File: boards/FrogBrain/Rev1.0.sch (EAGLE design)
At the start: 14 parts, among them U1 PIC16F1778, U2 AT25SF321, U3 ADP7104

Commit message: Final rev 1.0 brain and initial tadpole breadboard.
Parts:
- renumbered U$4 to SW
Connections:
- net GND: now also JP4.1, JP4.2, JP4.3, JP5.4, JP5.8
- net SCK: now also JP5.7; no longer JP4.3
- net SI: now also JP5.5; no longer JP4.5
- net SO: now also JP5.6; no longer JP4.4
- net UARTRX: now also JP4.4; no longer JP4.1
- net UARTTX: now also JP4.5; no longer JP4.2
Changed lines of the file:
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@@
 <part name="SUPPLY7" library="supply2" deviceset="GND" device=""/>
 <part name="R2" library="adafruit" deviceset="R-US_" device="R0805" value="100K"/>
-<part name="U$4" library="lib-works" deviceset="PTS645" device=""/>
+<part name="SW" library="lib-works" deviceset="PTS645" device=""/>
 <part name="SUPPLY8" library="supply2" deviceset="GND" device=""/>
 <part name="VDD2" library="supply1" deviceset="VDD" device=""/>
@@
 <instance part="SUPPLY7" gate="GND" x="2.54" y="53.34"/>
 <instance part="R2" gate="G$1" x="-50.8" y="76.2" rot="R90"/>
-<instance part="U$4" gate="G$1" x="-53.34" y="63.5"/>
+<instance part="SW" gate="G$1" x="-53.34" y="63.5"/>
 <instance part="SUPPLY8" gate="GND" x="-50.8" y="50.8"/>
 <instance part="VDD2" gate="G$1" x="-86.36" y="25.4"/>
@@
 </segment>
 <segment>
-<pinref part="U$4" gate="G$1" pin="P$2"/>
+<pinref part="SW" gate="G$1" pin="P$2"/>
 <pinref part="SUPPLY8" gate="GND" pin="GND"/>
-<pinref part="U$4" gate="G$1" pin="P$1"/>
+<pinref part="SW" gate="G$1" pin="P$1"/>
 <wire x1="-50.8" y1="55.88" x2="-53.34" y2="55.88" width="0.1524" layer="91"/>
 <wire x1="-50.8" y1="55.88" x2="-50.8" y2="53.34" width="0.1524" layer="91"/>
@@
 </segment>
 <segment>
-<wire x1="132.08" y1="5.08" x2="114.3" y2="5.08" width="0.1524" layer="91"/>
+<wire x1="132.08" y1="5.08" x2="124.46" y2="5.08" width="0.1524" layer="91"/>
+<wire x1="124.46" y1="5.08" x2="114.3" y2="5.08" width="0.1524" layer="91"/>
 <wire x1="114.3" y1="5.08" x2="114.3" y2="2.54" width="0.1524" layer="91"/>
 <pinref part="SUPPLY9" gate="GND" pin="GND"/>
 <pinref part="JP5" gate="G$1" pin="3"/>
+<pinref part="JP5" gate="G$1" pin="4"/>
+<wire x1="132.08" y1="2.54" x2="124.46" y2="2.54" width="0.1524" layer="91"/>
+<wire x1="124.46" y1="2.54" x2="124.46" y2="5.08" width="0.1524" layer="91"/>
+</segment>
+<segment>
+<wire x1="132.08" y1="43.18" x2="124.46" y2="43.18" width="0.1524" layer="91"/>
+<label x="124.46" y="43.18" size="1.27" layer="95" rot="R180" xref="yes"/>
+<pinref part="JP4" gate="G$1" pin="1"/>
+</segment>
+<segment>
+<wire x1="132.08" y1="40.64" x2="124.46" y2="40.64" width="0.1524" layer="91"/>
+<label x="124.46" y="40.64" size="1.27" layer="95" rot="R180" xref="yes"/>
+<pinref part="JP4" gate="G$1" pin="2"/>
+</segment>
+<segment>
+<wire x1="132.08" y1="38.1" x2="124.46" y2="38.1" width="0.1524" layer="91"/>
+<label x="124.46" y="38.1" size="1.27" layer="95" rot="R180" xref="yes"/>
+<pinref part="JP4" gate="G$1" pin="3"/>
+</segment>
+<segment>
+<pinref part="JP5" gate="G$1" pin="8"/>
+<wire x1="132.08" y1="-7.62" x2="124.46" y2="-7.62" width="0.1524" layer="91"/>
+<label x="124.46" y="-7.62" size="1.27" layer="95" rot="R180" xref="yes"/>
 </segment>
 </net>
@@
 <segment>
 <pinref part="R2" gate="G$1" pin="1"/>
-<pinref part="U$4" gate="G$1" pin="P$4"/>
+<pinref part="SW" gate="G$1" pin="P$4"/>
 <wire x1="-50.8" y1="71.12" x2="-45.72" y2="71.12" width="0.1524" layer="91"/>
 <wire x1="-45.72" y1="71.12" x2="-45.72" y2="73.66" width="0.1524" layer="91"/>
@@
 <wire x1="-45.72" y1="73.66" x2="-40.64" y2="73.66" width="0.1524" layer="91"/>
 <junction x="-50.8" y="71.12"/>
-<pinref part="U$4" gate="G$1" pin="P$3"/>
+<pinref part="SW" gate="G$1" pin="P$3"/>
 <wire x1="-50.8" y1="71.12" x2="-53.34" y2="71.12" width="0.1524" layer="91"/>
 </segment>
@@
 </segment>
 <segment>
-<wire x1="132.08" y1="43.18" x2="124.46" y2="43.18" width="0.1524" layer="91"/>
-<label x="124.46" y="43.18" size="1.27" layer="95" rot="R180" xref="yes"/>
-<pinref part="JP4" gate="G$1" pin="1"/>
+<wire x1="132.08" y1="35.56" x2="124.46" y2="35.56" width="0.1524" layer="91"/>
+<label x="124.46" y="35.56" size="1.27" layer="95" rot="R180" xref="yes"/>
+<pinref part="JP4" gate="G$1" pin="4"/>
 </segment>
 </net>
@@
 </segment>
 <segment>
-<wire x1="132.08" y1="40.64" x2="124.46" y2="40.64" width="0.1524" layer="91"/>
-<label x="124.46" y="40.64" size="1.27" layer="95" rot="R180" xref="yes"/>
-<pinref part="JP4" gate="G$1" pin="2"/>
+<wire x1="132.08" y1="33.02" x2="124.46" y2="33.02" width="0.1524" layer="91"/>
+<label x="124.46" y="33.02" size="1.27" layer="95" rot="R180" xref="yes"/>
+<pinref part="JP4" gate="G$1" pin="5"/>
 </segment>
 </net>
@@
 </segment>
 <segment>
-<wire x1="132.08" y1="38.1" x2="124.46" y2="38.1" width="0.1524" layer="91"/>
-<label x="124.46" y="38.1" size="1.27" layer="95" rot="R180" xref="yes"/>
-<pinref part="JP4" gate="G$1" pin="3"/>
+<pinref part="JP5" gate="G$1" pin="7"/>
+<wire x1="132.08" y1="-5.08" x2="124.46" y2="-5.08" width="0.1524" layer="91"/>
+<label x="124.46" y="-5.08" size="1.27" layer="95" rot="R180" xref="yes"/>
 </segment>
 </net>
@@
 </segment>
 <segment>
-<wire x1="132.08" y1="35.56" x2="124.46" y2="35.56" width="0.1524" layer="91"/>
-<label x="124.46" y="35.56" size="1.27" layer="95" rot="R180" xref="yes"/>
-<pinref part="JP4" gate="G$1" pin="4"/>
+<pinref part="JP5" gate="G$1" pin="6"/>
+<wire x1="132.08" y1="-2.54" x2="124.46" y2="-2.54" width="0.1524" layer="91"/>
+<label x="124.46" y="-2.54" size="1.27" layer="95" rot="R180" xref="yes"/>
 </segment>
 </net>
@@
 </segment>
 <segment>
-<wire x1="132.08" y1="33.02" x2="124.46" y2="33.02" width="0.1524" layer="91"/>
-<label x="124.46" y="33.02" size="1.27" layer="95" rot="R180" xref="yes"/>
-<pinref part="JP4" gate="G$1" pin="5"/>
-</segment>
-</net>
+<pinref part="JP5" gate="G$1" pin="5"/>
+<wire x1="132.08" y1="0" x2="124.46" y2="0" width="0.1524" layer="91"/>
+<label x="124.46" y="0" size="1.27" layer="95" rot="R180" xref="yes"/>
+</segment>
+</net>

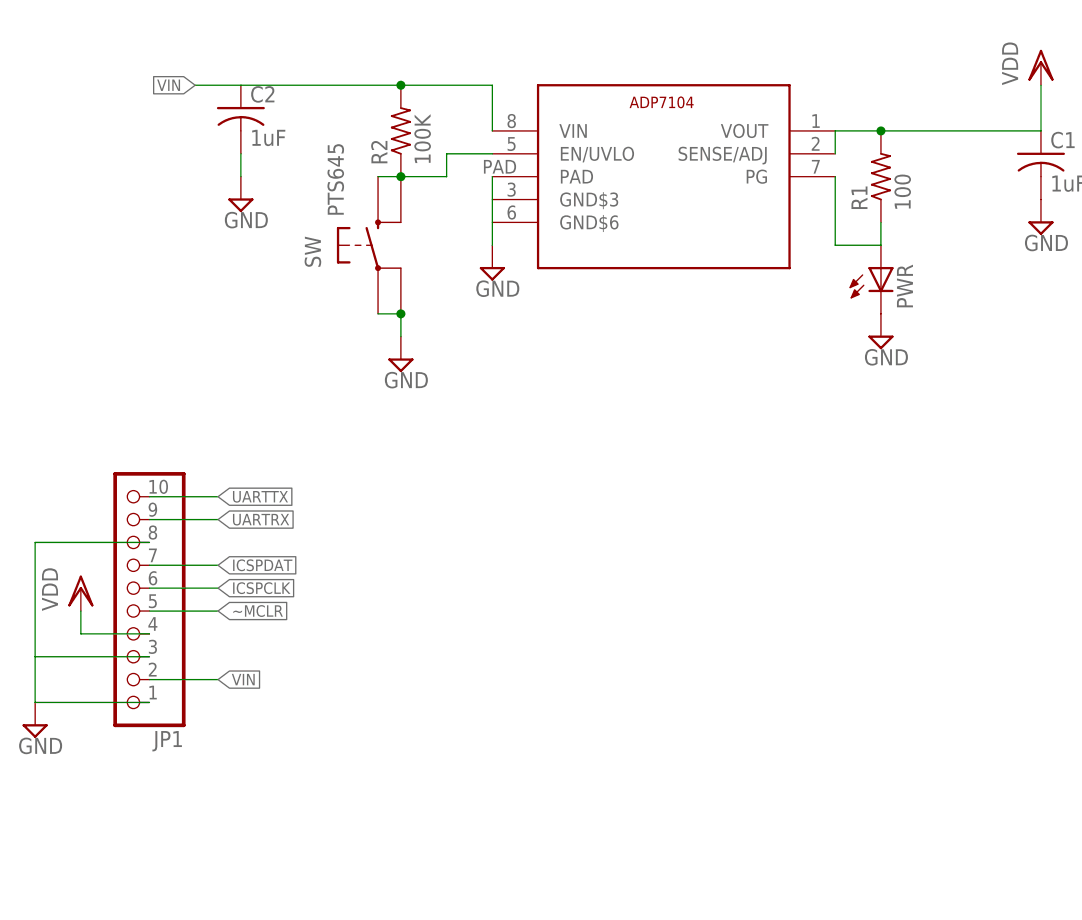
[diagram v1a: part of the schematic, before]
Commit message: Kermit PIC protocol and small frogbrain board mods.
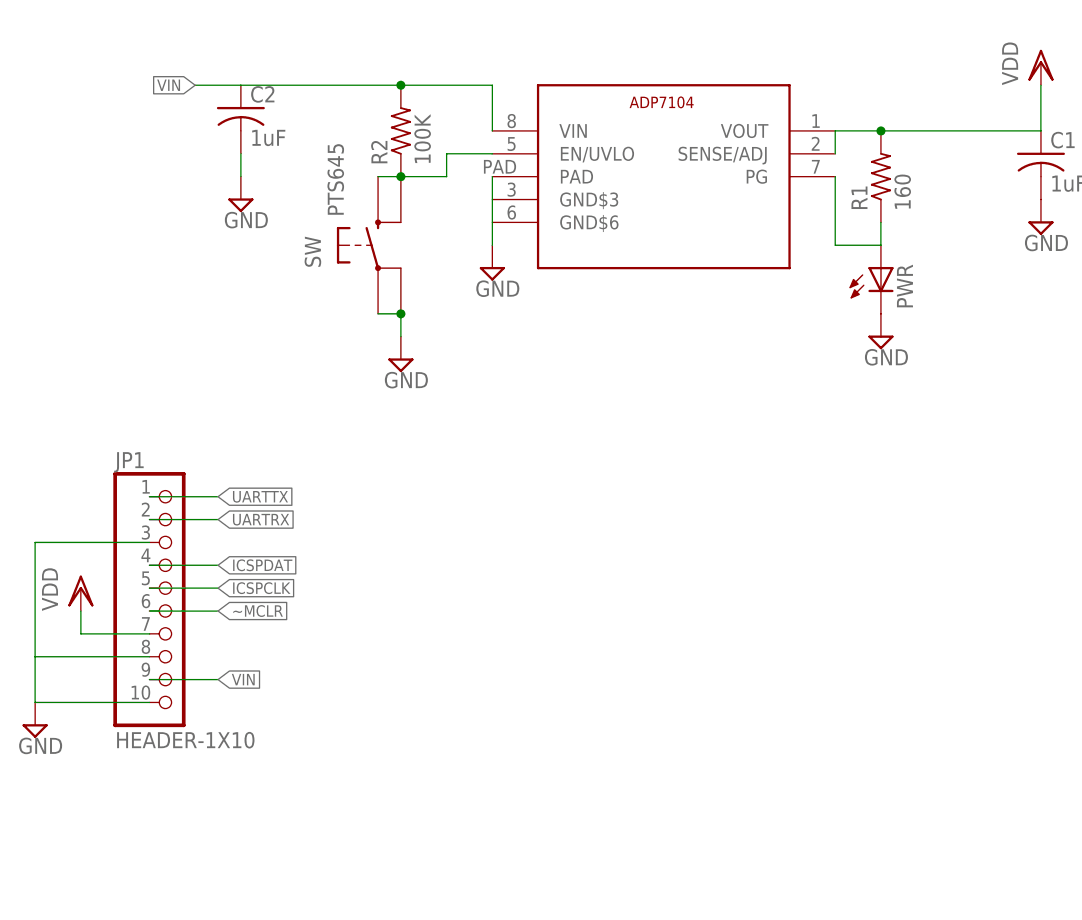
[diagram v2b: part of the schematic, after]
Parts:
- JP1: value (none) -> HEADER-1X10; device pinhead:PINHD-1X10 -> lib-works:HEADER-1X10
- R1: value 100 -> 160
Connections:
- net GND: now also JP1.10; no longer JP1.1
- net ICSPCLK: now also JP1.5; no longer JP1.6
- net ICSPDAT: now also JP1.4; no longer JP1.7
- net UARTRX: now also JP1.2; no longer JP1.9
- net UARTTX: now also JP1.1; no longer JP1.10
- net VDD: now also JP1.7; no longer JP1.4
- net VIN: now also JP1.9; no longer JP1.2
- net ~MCLR: now also JP1.6; no longer JP1.5
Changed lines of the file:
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@@
 <part name="SUPPLY4" library="supply2" deviceset="GND" device=""/>
 <part name="SUPPLY5" library="supply2" deviceset="GND" device=""/>
-<part name="JP1" library="pinhead" deviceset="PINHD-1X10" device=""/>
 <part name="VDD1" library="supply1" deviceset="VDD" device=""/>
 <part name="VDD3" library="supply1" deviceset="VDD" device=""/>
@@
 <part name="SUPPLY3" library="supply2" deviceset="GND" device=""/>
 <part name="PWR" library="adafruit" deviceset="LED" device="CHIP-LED0805"/>
-<part name="R1" library="adafruit" deviceset="R-US_" device="R0805" value="100"/>
+<part name="R1" library="adafruit" deviceset="R-US_" device="R0805" value="160"/>
 <part name="SUPPLY7" library="supply2" deviceset="GND" device=""/>
 <part name="R2" library="adafruit" deviceset="R-US_" device="R0805" value="100K"/>
@@
 <part name="JP4" library="lib-works" deviceset="HEADER-1X8" device=""/>
 <part name="JP5" library="lib-works" deviceset="HEADER-1X8" device=""/>
+<part name="JP1" library="lib-works" deviceset="HEADER-1X10" device=""/>
 </parts>
 <sheets>
@@
 <instance part="SUPPLY4" gate="GND" x="20.32" y="66.04"/>
 <instance part="SUPPLY5" gate="GND" x="-68.58" y="68.58"/>
-<instance part="JP1" gate="A" x="-81.28" y="22.86" rot="R180"/>
 <instance part="VDD1" gate="G$1" x="20.32" y="83.82"/>
 <instance part="VDD3" gate="G$1" x="38.1" y="83.82"/>
@@
 <instance part="JP4" gate="G$1" x="134.62" y="33.02"/>
 <instance part="JP5" gate="G$1" x="134.62" y="0"/>
+<instance part="JP1" gate="G$1" x="-76.2" y="25.4"/>
 </instances>
 <busses>
@@
 <wire x1="-91.44" y1="12.7" x2="-91.44" y2="17.78" width="0.1524" layer="91"/>
 <wire x1="-91.44" y1="17.78" x2="-78.74" y2="17.78" width="0.1524" layer="91"/>
-<pinref part="JP1" gate="A" pin="1"/>
-<pinref part="JP1" gate="A" pin="3"/>
 <wire x1="-91.44" y1="17.78" x2="-91.44" y2="30.48" width="0.1524" layer="91"/>
-<pinref part="JP1" gate="A" pin="8"/>
 <wire x1="-91.44" y1="30.48" x2="-78.74" y2="30.48" width="0.1524" layer="91"/>
+<pinref part="JP1" gate="G$1" pin="3"/>
+<pinref part="JP1" gate="G$1" pin="8"/>
+<pinref part="JP1" gate="G$1" pin="10"/>
 </segment>
 <segment>
@@
 <pinref part="VDD2" gate="G$1" pin="VDD"/>
 <wire x1="-86.36" y1="22.86" x2="-86.36" y2="20.32" width="0.1524" layer="91"/>
-<pinref part="JP1" gate="A" pin="4"/>
 <wire x1="-86.36" y1="20.32" x2="-78.74" y2="20.32" width="0.1524" layer="91"/>
+<pinref part="JP1" gate="G$1" pin="7"/>
 </segment>
 <segment>
@@
 <net name="~MCLR" class="0">
 <segment>
-<pinref part="JP1" gate="A" pin="5"/>
 <wire x1="-78.74" y1="22.86" x2="-71.12" y2="22.86" width="0.1524" layer="91"/>
 <label x="-71.12" y="22.86" size="1.27" layer="95" xref="yes"/>
+<pinref part="JP1" gate="G$1" pin="6"/>
 </segment>
 <segment>
@@
 <net name="ICSPCLK" class="0">
 <segment>
-<pinref part="JP1" gate="A" pin="6"/>
 <wire x1="-78.74" y1="25.4" x2="-71.12" y2="25.4" width="0.1524" layer="91"/>
 <label x="-71.12" y="25.4" size="1.27" layer="95" xref="yes"/>
+<pinref part="JP1" gate="G$1" pin="5"/>
 </segment>
 <segment>
@@
 <net name="ICSPDAT" class="0">
 <segment>
-<pinref part="JP1" gate="A" pin="7"/>
 <wire x1="-78.74" y1="27.94" x2="-71.12" y2="27.94" width="0.1524" layer="91"/>
 <label x="-71.12" y="27.94" size="1.27" layer="95" xref="yes"/>
+<pinref part="JP1" gate="G$1" pin="4"/>
 </segment>
 <segment>
@@
 <net name="UARTRX" class="0">
 <segment>
-<pinref part="JP1" gate="A" pin="9"/>
 <wire x1="-78.74" y1="33.02" x2="-71.12" y2="33.02" width="0.1524" layer="91"/>
 <label x="-71.12" y="33.02" size="1.27" layer="95" xref="yes"/>
+<pinref part="JP1" gate="G$1" pin="2"/>
 </segment>
 <segment>
@@
 <net name="UARTTX" class="0">
 <segment>
-<pinref part="JP1" gate="A" pin="10"/>
 <wire x1="-78.74" y1="35.56" x2="-71.12" y2="35.56" width="0.1524" layer="91"/>
 <label x="-71.12" y="35.56" size="1.27" layer="95" xref="yes"/>
+<pinref part="JP1" gate="G$1" pin="1"/>
 </segment>
 <segment>
@@
 <net name="VIN" class="0">
 <segment>
-<pinref part="JP1" gate="A" pin="2"/>
 <wire x1="-78.74" y1="15.24" x2="-71.12" y2="15.24" width="0.1524" layer="91"/>
 <label x="-71.12" y="15.24" size="1.27" layer="95" xref="yes"/>
-</segment>
-<segment>
+<pinref part="JP1" gate="G$1" pin="9"/>
+</segment>
+<segment>
